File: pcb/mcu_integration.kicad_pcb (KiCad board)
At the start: 4 copper layers, 90.2 x 95.9 mm, 106 parts, among them IC1 TL7660IDGKR, IC10 AD844_OPAMP_MEL, IC3 FOD814_OPTO_NOSHD, IC5 FOD814_OPTO_MEL, IC6 AD844_OPAMP_AL, IC7 FOD814_OPTO_AL, IC8 AD844_OPAMP_NOSHD, IC9 TL081IDT, J5 DM3BT-DSF-PEJS, M1 MountingHole_Pad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

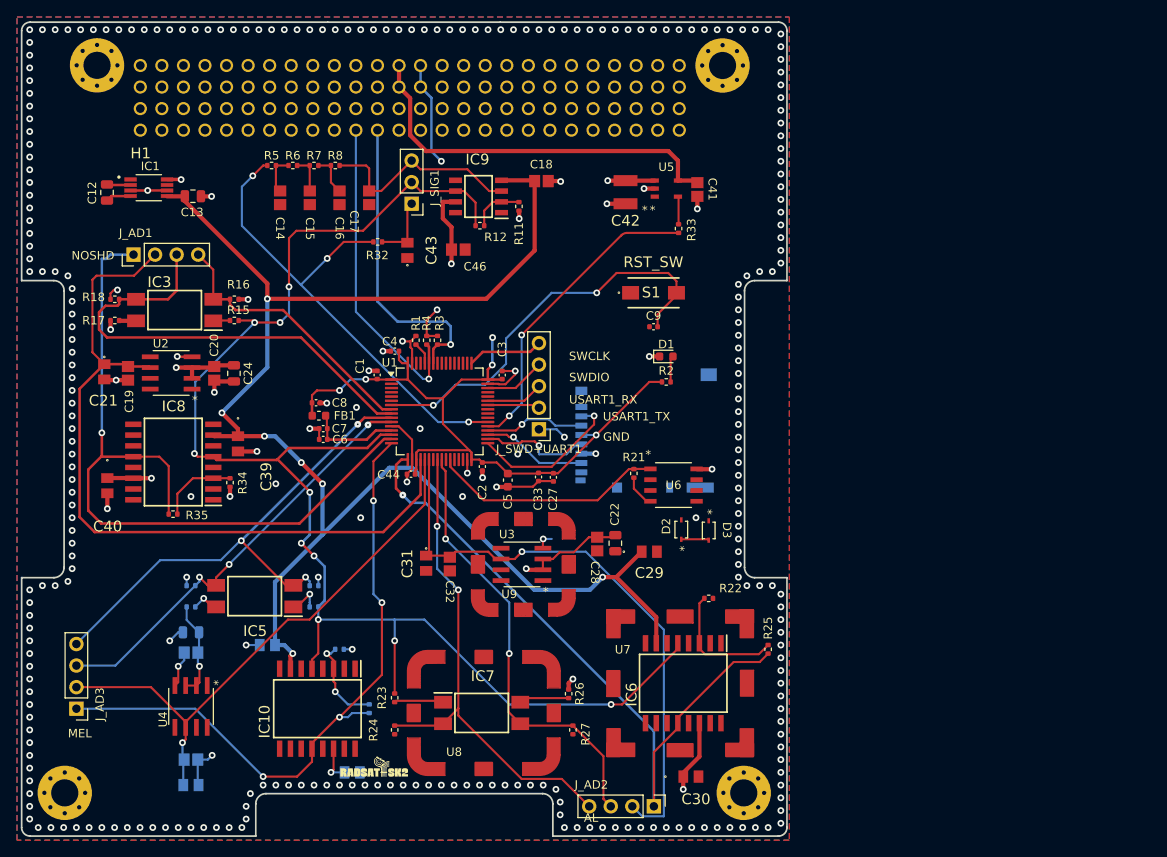
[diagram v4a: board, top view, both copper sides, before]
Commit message: Fixed Shield Solder Mask
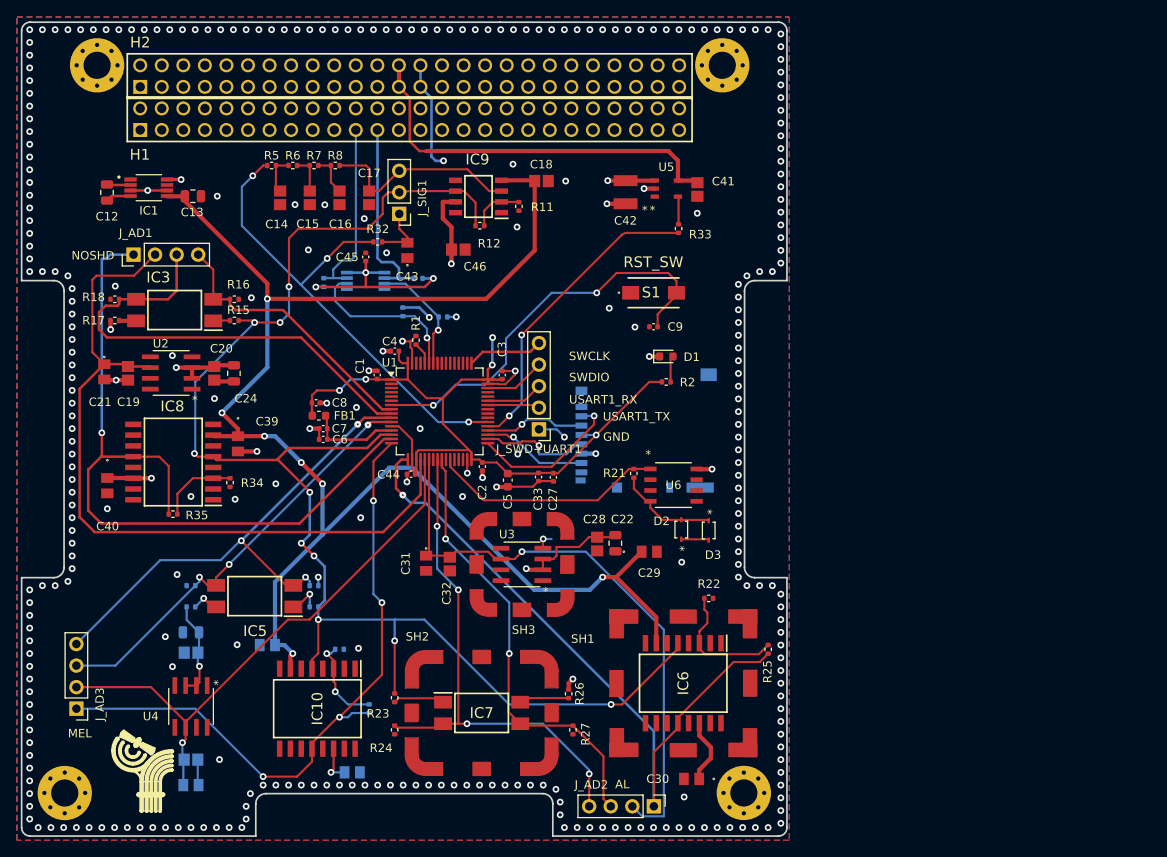
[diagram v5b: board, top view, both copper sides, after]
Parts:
- removed R3, R4: 2.2k, Resistor_SMD:R_0402_1005Metric
- removed U7: ~, capstone:AD844 Shield
- removed U9: ~, capstone:REF192 Shield
- added C45: 10n, Capacitor_SMD:C_0402_1005Metric, F.Cu at (133.1, 79.3)
- added R10: 10K, Resistor_SMD:R_0402_1005Metric, B.Cu at (137.5, 85.7)
- added R13: 10K, Resistor_SMD:R_0402_1005Metric, B.Cu at (139.3, 81.8)
- added R14: 10K, Resistor_SMD:R_0402_1005Metric, B.Cu at (128.2, 82.3)
- added R9: 10K, Resistor_SMD:R_0402_1005Metric, B.Cu at (142.2, 86.3)
- added SH1: ~, capstone:AD844 Shield, F.Cu at (170.5, 129.5)
- added SH2: ~, capstone:FOD814 Shield, F.Cu at (146.8, 133.0)
- added SH3: ~, capstone:REF192 Shield, F.Cu at (151.5, 115.5)
- H1, H2: footprint capstone:ESQ-126-Y-X-D -> capstone:RHDR52W64P254_2X26_6654X495X1135P; moved to F.Cu
- U8: value ~ -> LTC4300A-1IMS8_PBF; footprint capstone:FOD814 Shield -> capstone:LTC4300A-1IMS8_PBF; moved to B.Cu
- moved U8 52.8 mm to (133.1, 82.1)
- moved J_SIG1 1.89 mm to (137.0, 74.2)
- moved C30 0.28 mm to (171.5, 140.8), turned to 180 degrees
- turned H2 to 0 degrees
- turned H1 to 0 degrees
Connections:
- H1 pad 21: OBC_I2C_SDA -> I2C_SDA(2)
- H1 pad 23: OBC_I2C_SCL -> I2C_SCL(2)
- H2 pad 14: unconnected-(H2-Pad14) -> GND
- H2 pad 17: unconnected-(H2-Pad17) -> GND
- H2 pad 21: unconnected-(H2-Pad21) -> GND
- H2 pad 22: unconnected-(H2-Pad22) -> GND
- H2 pad 47: unconnected-(H2-Pad47) -> GND
- H2 pad 48: unconnected-(H2-Pad48) -> GND
- H2 pad 9: unconnected-(H2-Pad9) -> GND
- U8 pad 1: GND -> 3.3V Output
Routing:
- net 3.3V Output: track 101.6 -> 125.7 mm, vias 7 -> 11
- net I2C_SCL(2): track 0.00 -> 22.8 mm
- net OBC_I2C_SCL: track 36.1 -> 14.2 mm
- net I2C_SDA(2): track 0.00 -> 21.9 mm
- net OBC_I2C_SDA: track 37.5 -> 19.5 mm
- net GND: track 92.6 -> 75.2 mm, vias 301 -> 310
- net ADC1_IN14_OPTO_F_AL: track 59.4 -> 61.9 mm, vias 2 -> 4
- net Net-(J_SIG1-Pin_1): track 7.84 -> 6.83 mm
- net RC_OUTPUT: track 24.9 -> 24.0 mm
- net ADC1_IN0_SINE: track 174.0 -> 174.8 mm
- net +5V: track 72.7 -> 72.4 mm, vias 12 -> 11
- added copper zone on In2.Cu, net 3.3V Output
- removed copper zone on In1.Cu, net 3.3V Output

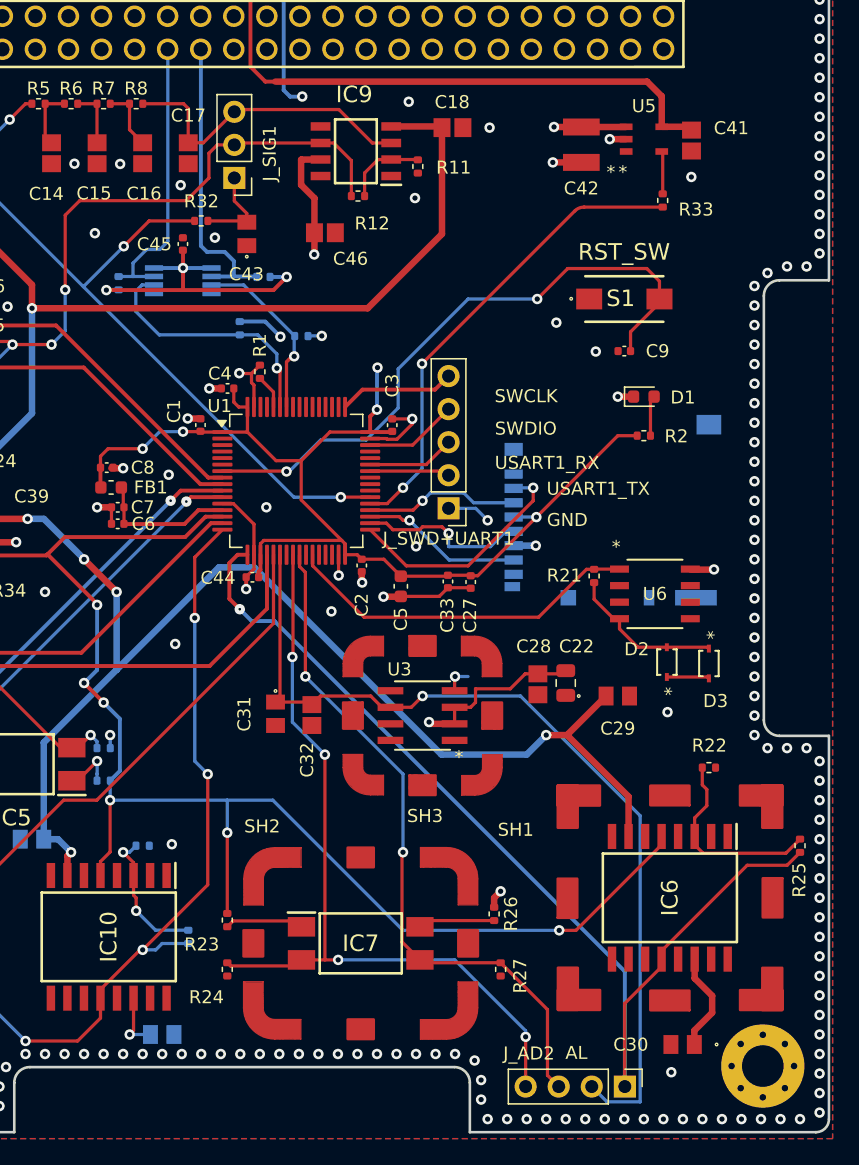
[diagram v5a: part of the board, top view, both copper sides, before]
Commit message: Moved resistors and capacitors to back of board
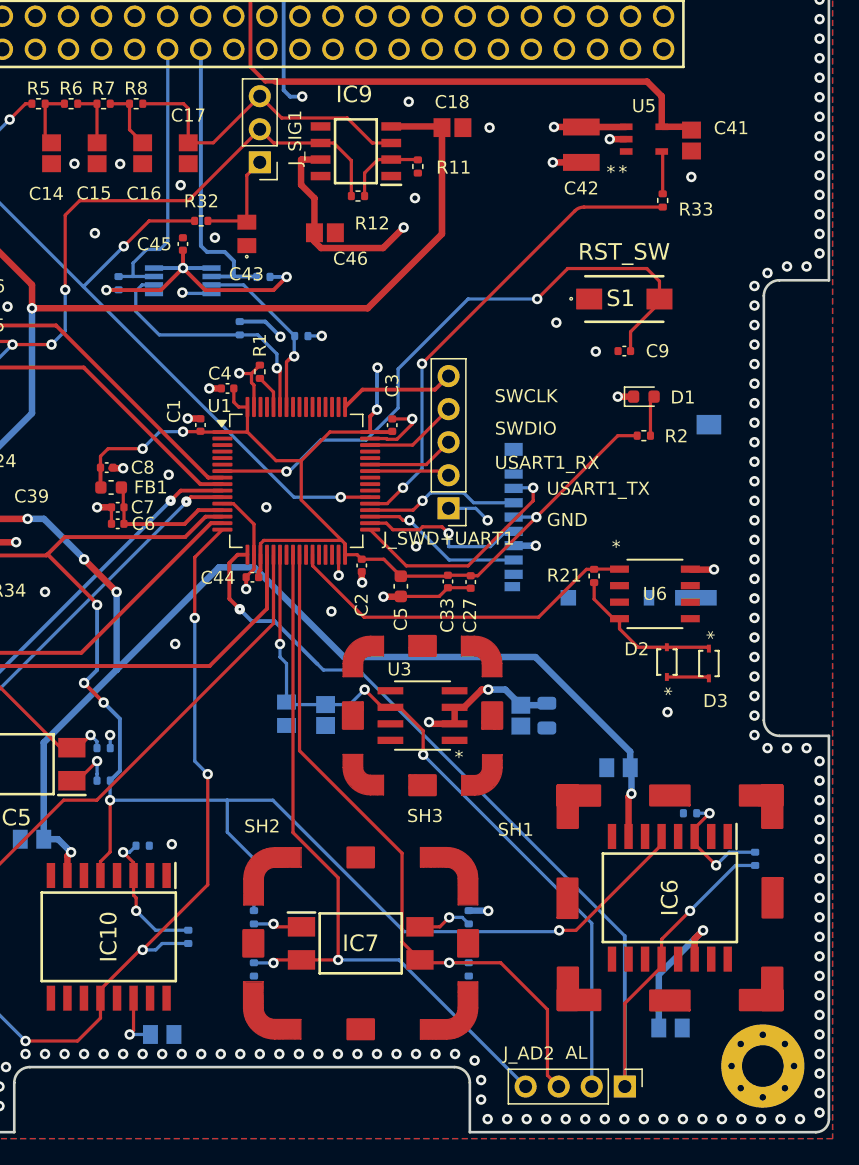
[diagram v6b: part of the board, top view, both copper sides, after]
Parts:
- C22, C28, C29, C30, C31, C32, R22, R23, R24, R25, R26, R27: moved to B.Cu
- moved C29 5.51 mm to (166.6, 119.5), turned to 180 degrees
- moved R22 3.79 mm to (172.1, 123.0), turned to 0 degrees
- moved R25 3.59 mm to (177.1, 126.5)
- moved C22 2.89 mm to (161.1, 115.5)
- moved C28 2.74 mm to (159.1, 115.5)
- moved R27 2.45 mm to (155.1, 135.0)
- moved J_SIG1 2.30 mm to (139.0, 73.0)
- moved R23 2.06 mm to (138.6, 131.0)
- moved R24 2.05 mm to (138.6, 135.0)
- moved R26 1.97 mm to (155.1, 131.0)
- moved C30 1.57 mm to (170.6, 139.5), turned to 0 degrees
- moved C32 1.05 mm to (144.1, 115.5)
- moved C31 0.84 mm to (141.1, 115.4)
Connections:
- H2 pad 14: GND -> unconnected-(H2-Pad14)
- H2 pad 17: GND -> unconnected-(H2-Pad17)
- H2 pad 21: GND -> unconnected-(H2-Pad21)
- H2 pad 22: GND -> unconnected-(H2-Pad22)
- H2 pad 9: GND -> unconnected-(H2-Pad9)
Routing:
- net ADC1_IN6_VREF_AL: track 70.5 -> 57.2 mm, vias 1 -> 3
- net +5V: track 72.4 -> 80.8 mm, vias 11 -> 13
- net Net-(IC6--IN): track 15.3 -> 10.2 mm, vias 0 -> 2
- net ADC1_IN14_OPTO_F_AL: track 61.9 -> 58.2 mm, vias 4 -> 2
- net -5V Output: track 182.9 -> 179.6 mm
- net ADC1_IN3_OPAMP_AL: track 80.8 -> 79.1 mm, vias 1 -> 2
- net Net-(IC7-AK): track 6.54 -> 4.85 mm, vias 0 -> 1
- net ADC1_IN15_OPTO_E_AL: track 52.7 -> 54.1 mm, vias 2 -> 1
- net Net-(J_SIG1-Pin_1): track 6.83 -> 8.05 mm
- net Net-(IC7-C): track 7.06 -> 6.10 mm, vias 0 -> 1
- net RC_OUTPUT: track 24.0 -> 24.9 mm
- net GND: track 75.2 -> 75.3 mm, vias 310 -> 309
- net ADC1_IN0_SINE: track 174.8 -> 174.7 mm, vias 10 -> 9
